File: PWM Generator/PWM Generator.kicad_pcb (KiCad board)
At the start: 2 copper layers, 15 parts, among them J1 Screw_Terminal_01x02, J2 Screw_Terminal_01x02, Q1 IRF3205, U1 LM358, U2 LM7805_TO220

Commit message: first wire
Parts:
- moved R3 5.24 mm to (121.9, 80.0), turned to 180 degrees
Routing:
- net +5V: track 0.00 -> 78.5 mm
- net Net-(R1-Pad2): track 0.00 -> 21.8 mm
- net (no net): track 0.00 -> 2.54 mm

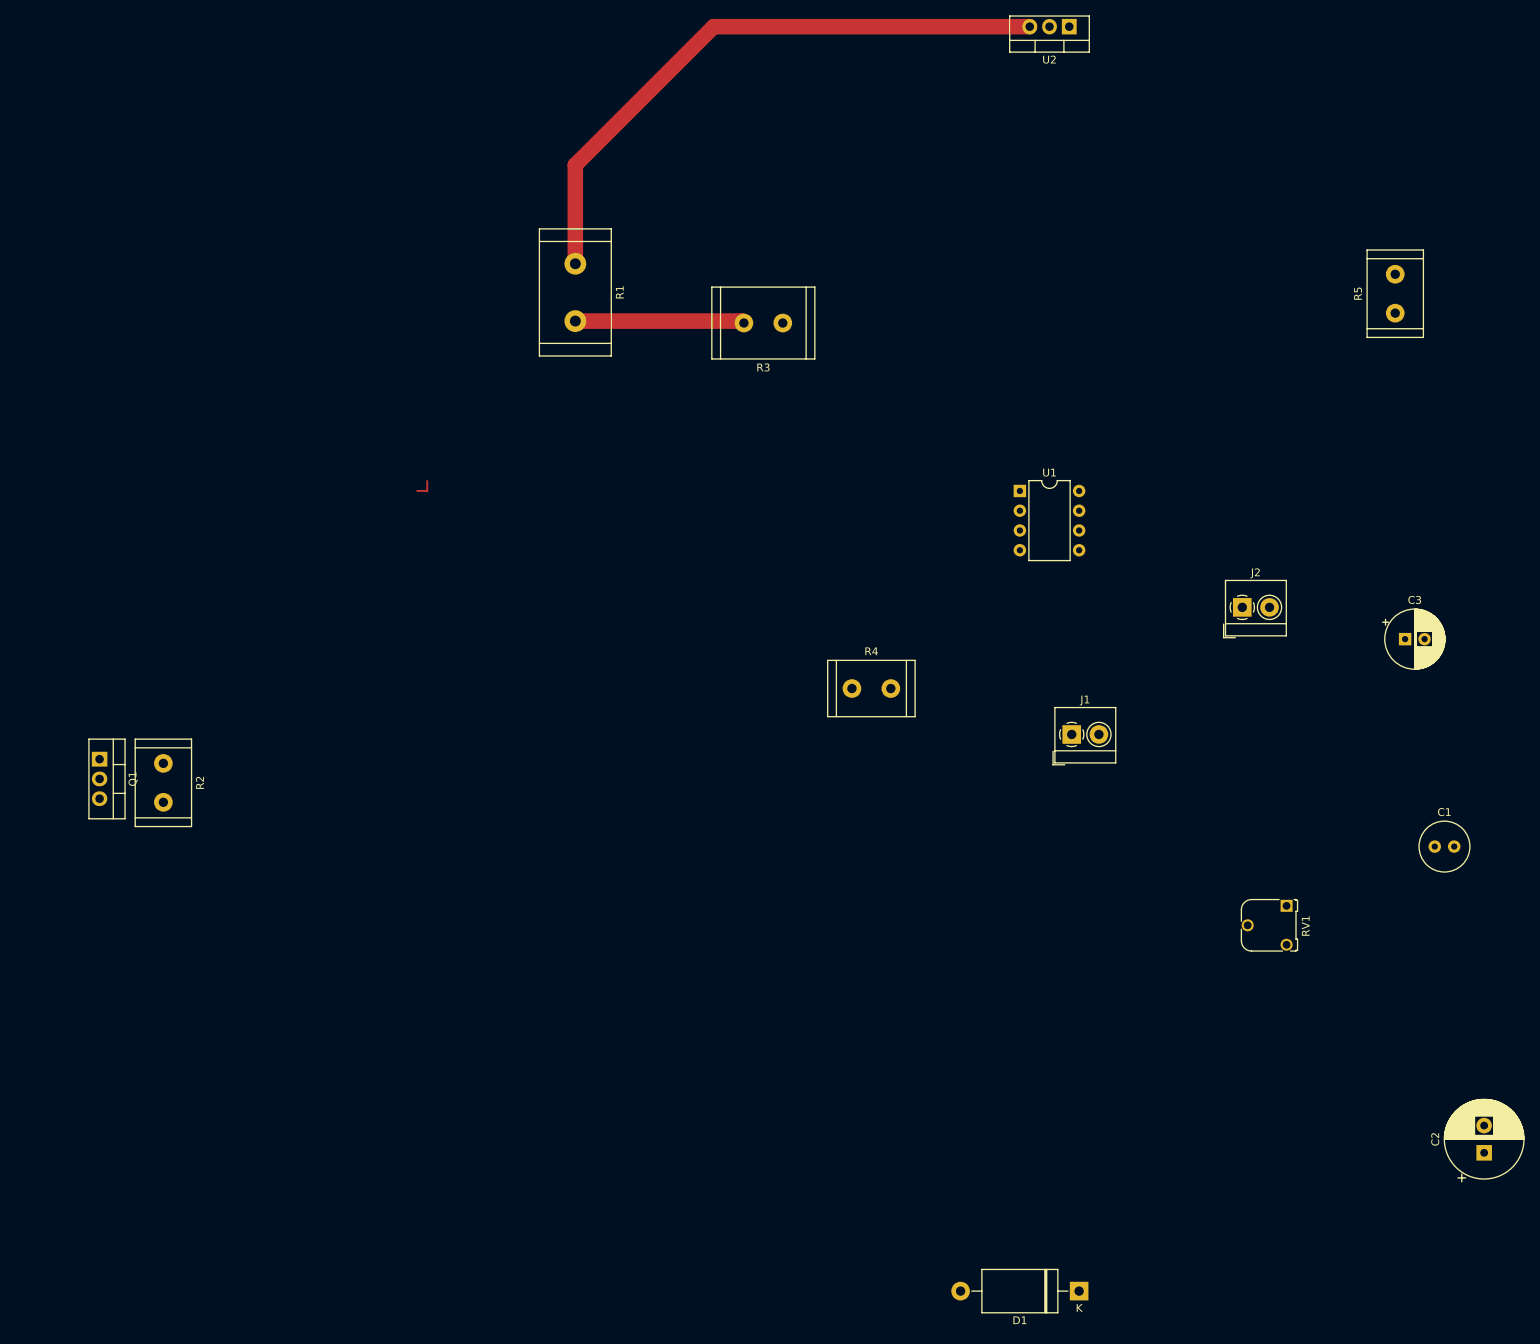
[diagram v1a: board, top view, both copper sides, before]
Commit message: edge boarder
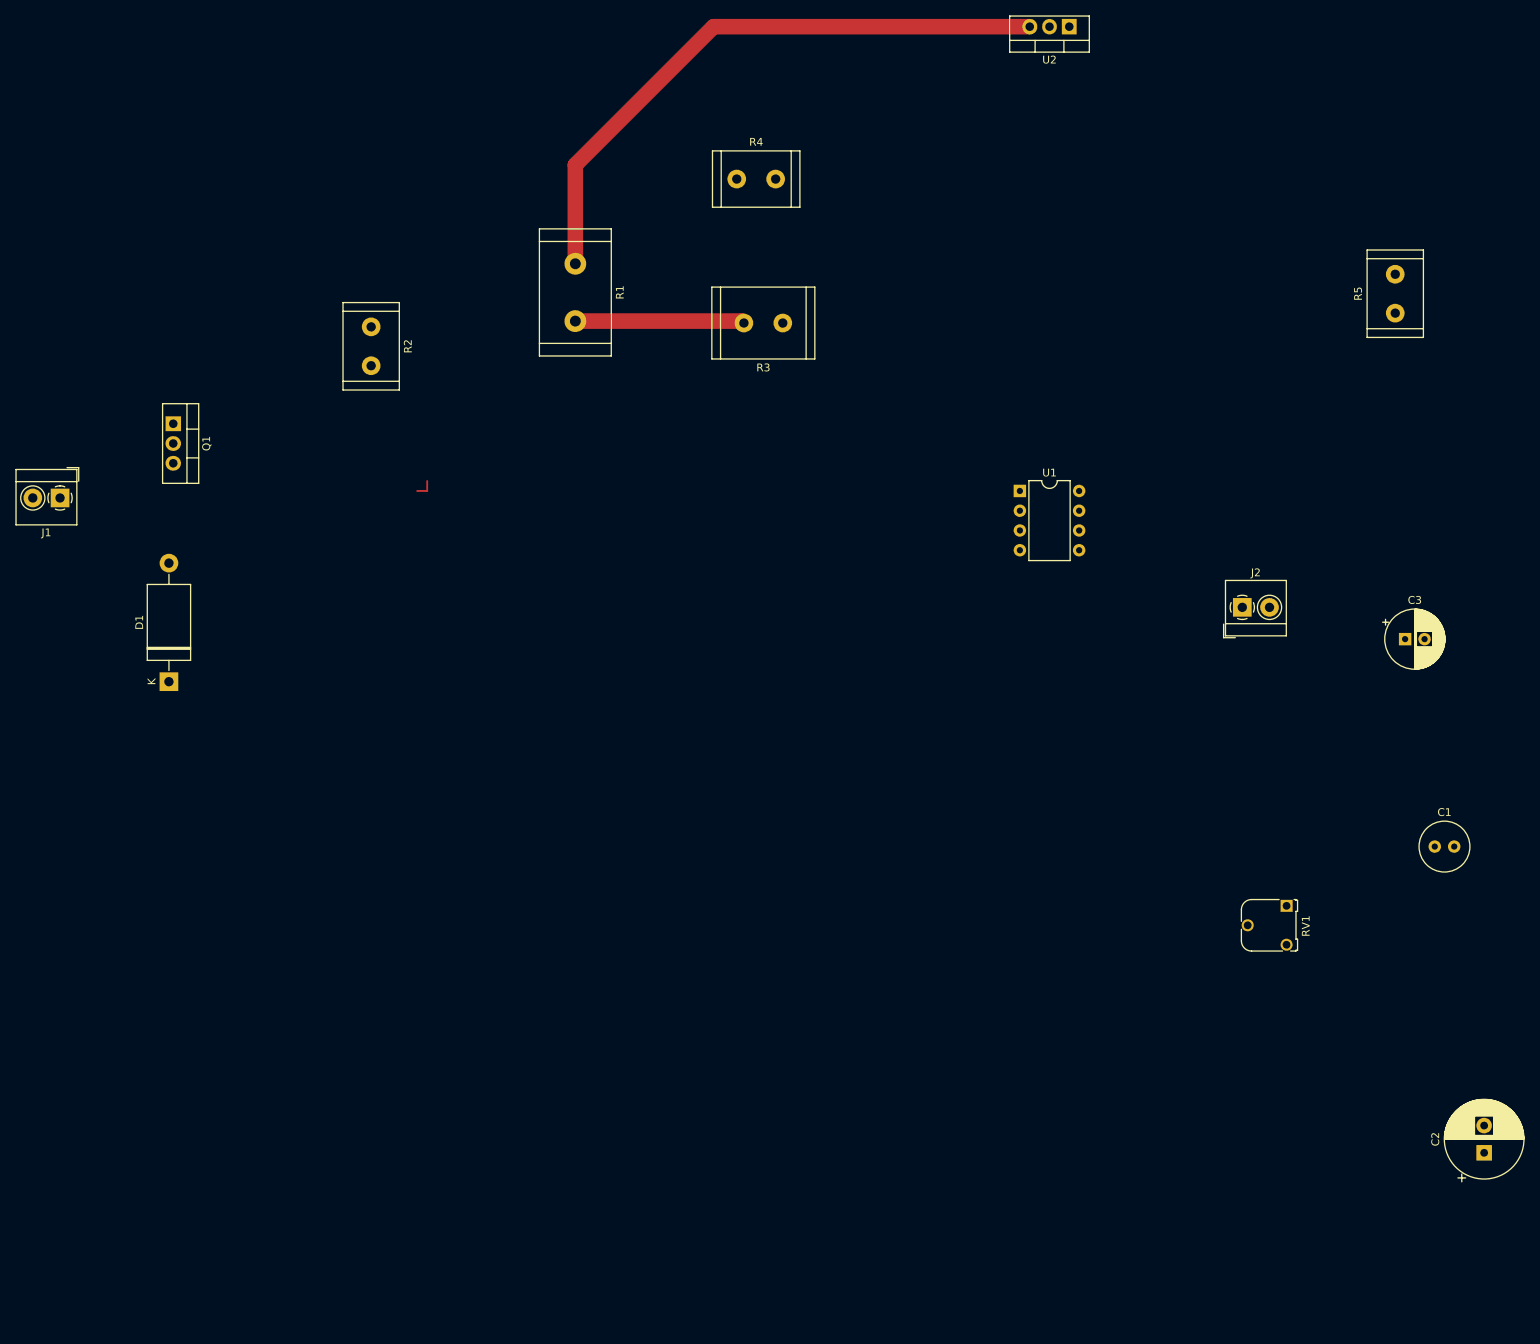
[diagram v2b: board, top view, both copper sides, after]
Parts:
- moved D1 140.8 mm to (43.0, 126.1), turned to 90 degrees
- moved J1 133.6 mm to (29.0, 102.5), turned to 180 degrees
- moved R4 67.2 mm to (116.0, 61.5)
- moved R2 62.2 mm to (69.0, 80.5)
- moved Q1 44.2 mm to (43.6, 93.0)
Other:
- net class Default removed
